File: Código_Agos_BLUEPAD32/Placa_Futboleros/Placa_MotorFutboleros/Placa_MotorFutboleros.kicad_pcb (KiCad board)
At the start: 2 copper layers, 25 x 25 mm, 1 part

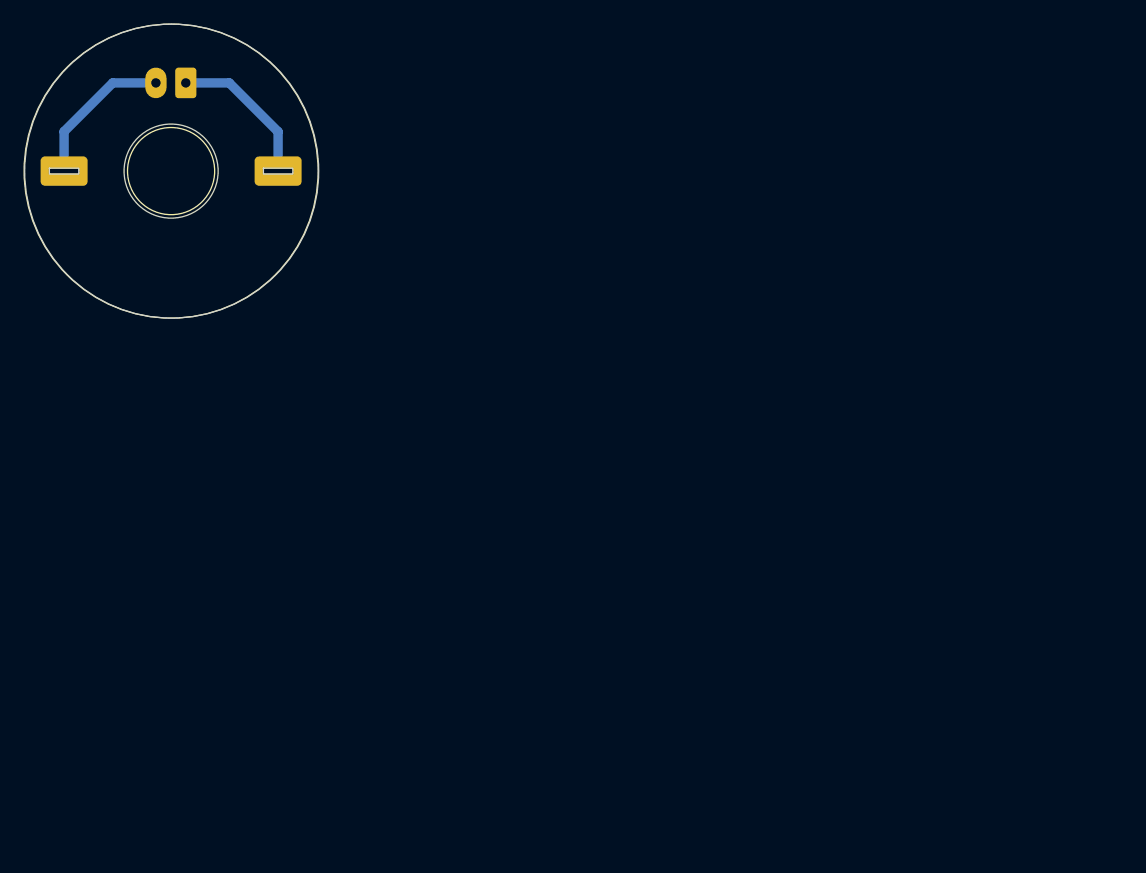
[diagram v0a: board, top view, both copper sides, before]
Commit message: Reorganización de carpetas
Se reordena algunas carpetas para mayor entendimiento...

También se adiciona el archivo original con links importantes
que contienen la información desde donde se empezó este proyecto.
> Tener en cuenta que algunos links pueden ya no estar disponibles, revisar.
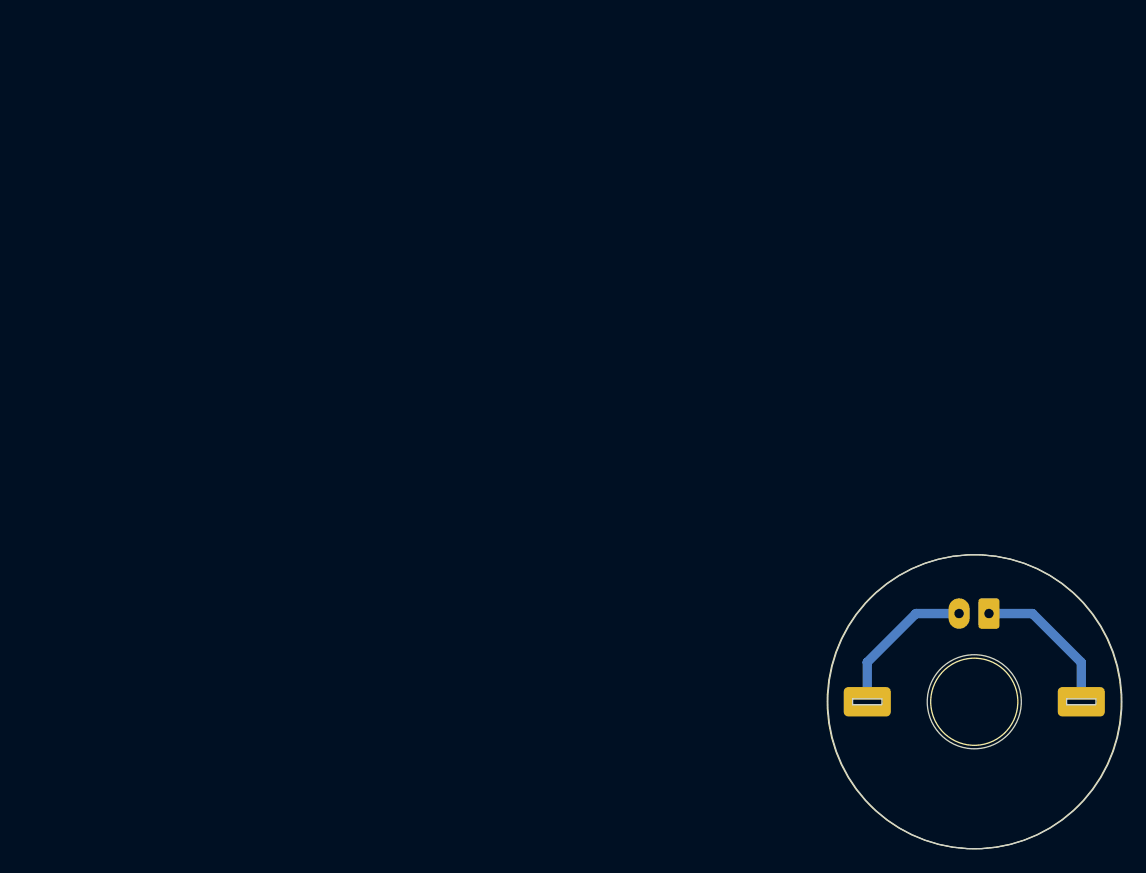
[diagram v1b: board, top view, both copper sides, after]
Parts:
- moved U1 81.9 mm to (157.1, 108.6)
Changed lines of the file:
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@@
 	(footprint "LibreríaMotor_Huella:Motor_JGA25-370"
 		(layer "F.Cu")
-		(at 88.844 63.444)
+		(at 157.143 108.569)
 		(property "Reference" "U1"
 			(at 0 6.5 0)
@@
 	)
 	(segment
-		(start 79.744 60.083)
-		(end 79.744 62.444)
+		(start 148.043 105.208)
+		(end 148.043 107.569)
 		(width 0.8)
 		(layer "B.Cu")
@@
 	)
 	(segment
-		(start 83.883 55.944)
-		(end 79.744 60.083)
+		(start 152.182 101.069)
+		(end 148.043 105.208)
 		(width 0.8)
 		(layer "B.Cu")
@@
 	)
 	(segment
-		(start 87.554 55.944)
-		(end 83.883 55.944)
+		(start 155.853 101.069)
+		(end 152.182 101.069)
 		(width 0.8)
 		(layer "B.Cu")
@@
 	)
 	(segment
-		(start 90.094 55.944)
-		(end 93.79 55.944)
+		(start 158.393 101.069)
+		(end 162.089 101.069)
 		(width 0.8)
 		(layer "B.Cu")
@@
 	)
 	(segment
-		(start 97.944 60.098)
-		(end 97.944 62.444)
+		(start 166.243 105.223)
+		(end 166.243 107.569)
 		(width 0.8)
 		(layer "B.Cu")
@@
 	)
 	(segment
-		(start 93.79 55.944)
-		(end 97.944 60.098)
-		(width 0.8)
-		(layer "B.Cu")
+		(start 162.089 101.069)
+		(end 166.243 105.223)
+		(width 0.8)
+		(layer "B.Cu")
